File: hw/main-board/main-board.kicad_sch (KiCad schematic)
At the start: 66 parts, among them J1 USB_C_Receptacle_USB2.0_16P, J2 S4B-XH-A_LF__SN_, J3 S4B-XH-A_LF__SN_, J4 Conn_ARM_JTAG_SWD_10, Q1 AONR21307, U1 HUSB238_xxxDD, U2 AP63205WU, U3 AP2112K-3.3, U4 PTR54L, U5 TMC2226-SA, U6 TMC2226-SA, U7 KTD2026BEWE-TR

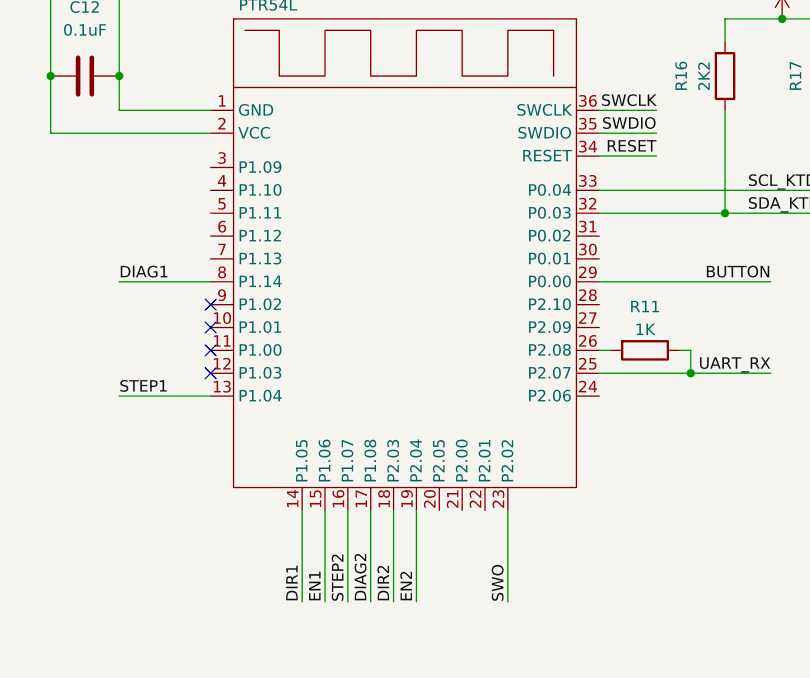
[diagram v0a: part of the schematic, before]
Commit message: Add not-connected labels
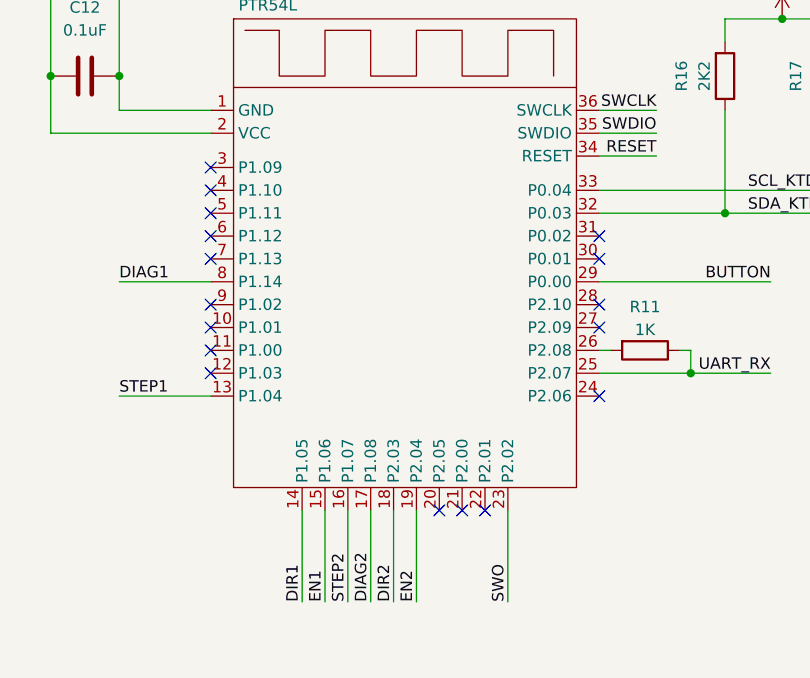
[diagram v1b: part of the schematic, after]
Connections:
- no-connect marks 16 -> 29
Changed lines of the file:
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@@
+	)
+	(no_connect
+		(at 243.84 63.5)
 	)
 	(no_connect
 		(at 92.71 109.22)
+	)
+	(no_connect
+		(at 287.02 88.9)
 	)
 	(no_connect
@@
 	)
 	(no_connect
+		(at 243.84 71.12)
+	)
+	(no_connect
+		(at 243.84 66.04)
+	)
+	(no_connect
+		(at 274.32 101.6)
+	)
+	(no_connect
+		(at 269.24 101.6)
+	)
+	(no_connect
+		(at 243.84 68.58)
+	)
+	(no_connect
 		(at 316.23 213.36)
 	)
@@
 	)
 	(no_connect
+		(at 271.78 101.6)
+	)
+	(no_connect
 		(at 243.84 83.82)
+	)
+	(no_connect
+		(at 287.02 73.66)
 	)
 	(no_connect
@@
 	)
 	(no_connect
+		(at 243.84 73.66)
+	)
+	(no_connect
+		(at 287.02 78.74)
+	)
+	(no_connect
 		(at 215.9 231.14)
 	)
@@
 	)
 	(no_connect
+		(at 287.02 81.28)
+	)
+	(no_connect
+		(at 287.02 71.12)
+	)
+	(no_connect

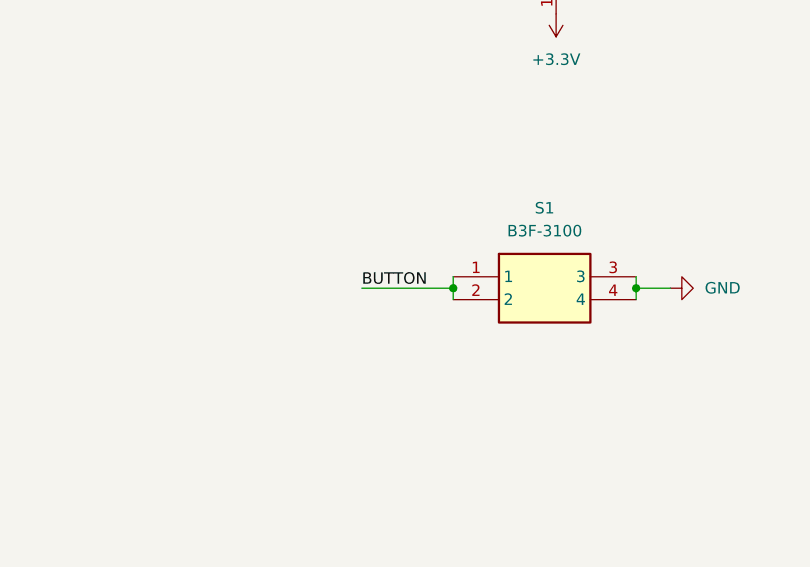
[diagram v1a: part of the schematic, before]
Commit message: Fix button pinout
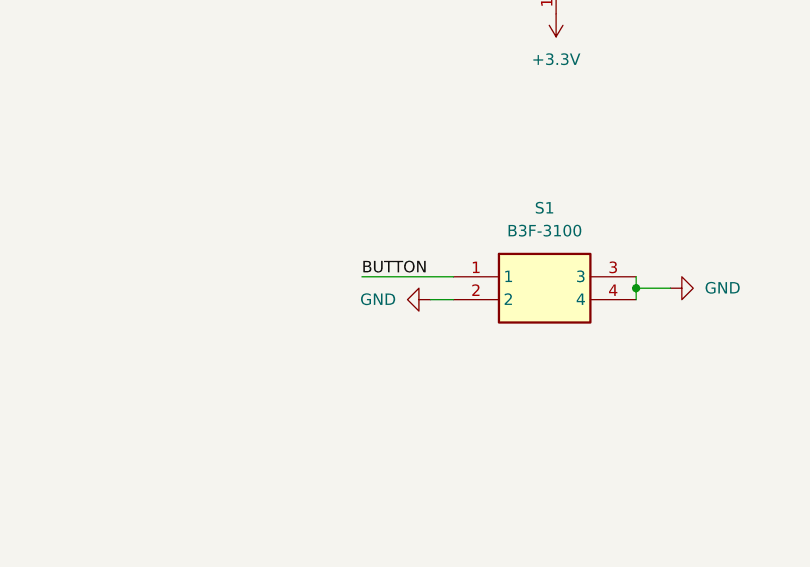
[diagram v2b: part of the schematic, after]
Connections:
- net BUTTON: no longer S1.2
- net GND: now also S1.2
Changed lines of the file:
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@@
 	)
 	(junction
-		(at 356.87 107.95)
-		(diameter 0)
-		(color 0 0 0 0)
-	)
-	(junction
 		(at 96.52 80.01)
 		(diameter 0)
@@
 	(wire
 		(pts
-			(xy 356.87 107.95) (xy 356.87 109.22)
-		)
-		(stroke
-			(width 0)
-			(type default)
-		)
-	)
-	(wire
-		(pts
 			(xy 215.9 160.02) (xy 218.44 160.02)
 		)
@@
 	(wire
 		(pts
-			(xy 346.71 107.95) (xy 356.87 107.95)
-		)
-		(stroke
-			(width 0)
-			(type default)
-		)
-	)
-	(wire
-		(pts
 			(xy 346.71 182.88) (xy 368.3 182.88)
 		)
@@
 	(wire
 		(pts
-			(xy 60.96 152.4) (xy 68.58 152.4)
+			(xy 354.33 109.22) (xy 356.87 109.22)
 		)
 		(stroke
@@
 	(wire
 		(pts
-			(xy 229.87 215.9) (xy 228.6 215.9)
+			(xy 60.96 152.4) (xy 68.58 152.4)
 		)
 		(stroke
@@
 	(wire
 		(pts
-			(xy 50.8 152.4) (xy 60.96 152.4)
+			(xy 229.87 215.9) (xy 228.6 215.9)
 		)
 		(stroke
@@
 	(wire
 		(pts
-			(xy 300.99 49.53) (xy 300.99 46.99)
+			(xy 50.8 152.4) (xy 60.96 152.4)
 		)
 		(stroke
@@
 	(wire
 		(pts
-			(xy 350.52 160.02) (xy 363.22 160.02)
+			(xy 300.99 49.53) (xy 300.99 46.99)
 		)
 		(stroke
@@
 	(wire
 		(pts
-			(xy 77.47 232.41) (xy 81.28 232.41)
+			(xy 350.52 160.02) (xy 363.22 160.02)
 		)
 		(stroke
@@
 	(wire
 		(pts
-			(xy 129.54 152.4) (xy 129.54 154.94)
+			(xy 77.47 232.41) (xy 81.28 232.41)
 		)
 		(stroke
@@
 	(wire
 		(pts
-			(xy 356.87 106.68) (xy 356.87 107.95)
+			(xy 129.54 152.4) (xy 129.54 154.94)
 		)
 		(stroke
@@
 	(wire
 		(pts
+			(xy 346.71 106.68) (xy 356.87 106.68)
+		)
+		(stroke
+			(width 0)
+			(type default)
+		)
+	)
+	(wire
+		(pts
 			(xy 250.19 187.96) (xy 250.19 189.23)
 		)
@@
 	)
 	(label "BUTTON"
-		(at 346.71 107.95 0)
+		(at 346.71 106.68 0)
 		(effects
 			(font
@@
 					(unit 1)
 				)
+			)
+		)
+	)
+	(symbol
+		(lib_id "power:GND")
+		(at 354.33 109.22 270)
+		(unit 1)
+		(body_style 1)
+		(exclude_from_sim no)
+		(in_bom yes)
+		(on_board yes)
+		(in_pos_files yes)
+		(dnp no)
+		(fields_autoplaced yes)
+		(property "Reference" "#PWR057"
+			(at 347.98 109.22 0)
+			(hide yes)
+			(show_name no)
+			(do_not_autoplace no)
+			(effects
+				(font
+					(size 1.27 1.27)
+				)
+			)
+		)
+		(property "Value" "GND"
+			(at 350.52 109.2199 90)
+			(show_name no)
+			(do_not_autoplace no)
+			(effects
+				(font
+					(size 1.27 1.27)
+				)
+				(justify right)
+			)
+		)
+		(property "Footprint" ""
+			(at 354.33 109.22 0)
+			(hide yes)
+			(show_name no)
+			(do_not_autoplace no)
+			(effects
+				(font
+					(size 1.27 1.27)
+				)
+			)
+		)
+		(property "Datasheet" ""
+			(at 354.33 109.22 0)
+			(hide yes)
+			(show_name no)
+			(do_not_autoplace no)
+			(effects
+				(font
+					(size 1.27 1.27)
+				)
+			)
+		)
+		(property "Description" "Power symbol creates a global label with name \"GND\" , ground"
+			(at 354.33 109.22 0)
+			(hide yes)
+			(show_name no)
+			(do_not_autoplace no)
+			(effects
+				(font
+					(size 1.27 1.27)
+				)
+			)
+		)
+		(pin "1"
+		)
+		(instances
+			(project "main-board"
+				(path "/fe215afa-a228-4dbb-8560-a0753323a3f2"
+					(reference "#PWR057")
+					(unit 1)
+				)

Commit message: Fix LED power source
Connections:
- net +3.3V: no longer C36.1, LED1.1, U7.5 (VIN)
- net +5V: now also C36.1, LED1.1, U7.5 (VIN)
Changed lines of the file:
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@@
 	)
 	(junction
-		(at 133.35 119.38)
-		(diameter 0)
-		(color 0 0 0 0)
-	)
-	(junction
 		(at 135.89 44.45)
 		(diameter 0)
@@
 	)
 	(junction
+		(at 133.35 119.38)
+		(diameter 0)
+		(color 0 0 0 0)
+	)
+	(junction
 		(at 50.8 160.02)
 		(diameter 0)
@@
 	)
 	(symbol
+		(lib_id "power:+5V")
+		(at 133.35 119.38 270)
+		(unit 1)
+		(body_style 1)
+		(exclude_from_sim no)
+		(in_bom yes)
+		(on_board yes)
+		(in_pos_files yes)
+		(dnp no)
+		(fields_autoplaced yes)
+		(property "Reference" "#PWR051"
+			(at 129.54 119.38 0)
+			(hide yes)
+			(show_name no)
+			(do_not_autoplace no)
+			(effects
+				(font
+					(size 1.27 1.27)
+				)
+			)
+		)
+		(property "Value" "+5V"
+			(at 137.16 119.3799 90)
+			(show_name no)
+			(do_not_autoplace no)
+			(effects
+				(font
+					(size 1.27 1.27)
+				)
+				(justify left)
+			)
+		)
+		(property "Footprint" ""
+			(at 133.35 119.38 0)
+			(hide yes)
+			(show_name no)
+			(do_not_autoplace no)
+			(effects
+				(font
+					(size 1.27 1.27)
+				)
+			)
+		)
+		(property "Datasheet" ""
+			(at 133.35 119.38 0)
+			(hide yes)
+			(show_name no)
+			(do_not_autoplace no)
+			(effects
+				(font
+					(size 1.27 1.27)
+				)
+			)
+		)
+		(property "Description" "Power symbol creates a global label with name \"+5V\""
+			(at 133.35 119.38 0)
+			(hide yes)
+			(show_name no)
+			(do_not_autoplace no)
+			(effects
+				(font
+					(size 1.27 1.27)
+				)
+			)
+		)
+		(pin "1"
+		)
+		(instances
+			(project "main-board"
+				(path "/fe215afa-a228-4dbb-8560-a0753323a3f2"
+					(reference "#PWR051")
+					(unit 1)
+				)
+			)
+		)
+	)
+	(symbol
 		(lib_id "power:GND")
 		(at 350.52 166.37 180)
@@
 	)
 	(symbol
+		(lib_id "power:+5V")
+		(at 186.69 124.46 270)
+		(unit 1)
+		(body_style 1)
+		(exclude_from_sim no)
+		(in_bom yes)
+		(on_board yes)
+		(in_pos_files yes)
+		(dnp no)
+		(fields_autoplaced yes)
+		(property "Reference" "#PWR052"
+			(at 182.88 124.46 0)
+			(hide yes)
+			(show_name no)
+			(do_not_autoplace no)
+			(effects
+				(font
+					(size 1.27 1.27)
+				)
+			)
+		)
+		(property "Value" "+5V"
+			(at 190.5 124.4599 90)
+			(show_name no)
+			(do_not_autoplace no)
+			(effects
+				(font
+					(size 1.27 1.27)
+				)
+				(justify left)
+			)
+		)
+		(property "Footprint" ""
+			(at 186.69 124.46 0)
+			(hide yes)
+			(show_name no)
+			(do_not_autoplace no)
+			(effects
+				(font
+					(size 1.27 1.27)
+				)
+			)
+		)
+		(property "Datasheet" ""
+			(at 186.69 124.46 0)
+			(hide yes)
+			(show_name no)
+			(do_not_autoplace no)
+			(effects
+				(font
+					(size 1.27 1.27)
+				)
+			)
+		)
+		(property "Description" "Power symbol creates a global label with name \"+5V\""
+			(at 186.69 124.46 0)
+			(hide yes)
+			(show_name no)
+			(do_not_autoplace no)
+			(effects
+				(font
+					(size 1.27 1.27)
+				)
+			)
+		)
+		(pin "1"
+		)
+		(instances
+			(project "main-board"
+				(path "/fe215afa-a228-4dbb-8560-a0753323a3f2"
+					(reference "#PWR052")
+					(unit 1)
+				)
+			)
+		)
+	)
+	(symbol
 		(lib_id "power:+3.3V")
 		(at 226.06 41.91 90)
@@
 	)
 	(symbol
-		(lib_id "power:+3.3V")
-		(at 133.35 119.38 270)
-		(unit 1)
-		(body_style 1)
-		(exclude_from_sim no)
-		(in_bom yes)
-		(on_board yes)
-		(in_pos_files yes)
-		(dnp no)
-		(fields_autoplaced yes)
-		(property "Reference" "#PWR052"
-			(at 129.54 119.38 0)
-			(hide yes)
-			(show_name no)
-			(do_not_autoplace no)
-			(effects
-				(font
-					(size 1.27 1.27)
-				)
-			)
-		)
-		(property "Value" "+3.3V"
-			(at 137.16 119.3799 90)
-			(show_name no)
-			(do_not_autoplace no)
-			(effects
-				(font
-					(size 1.27 1.27)
-				)
-				(justify left)
-			)
-		)
-		(property "Footprint" ""
-			(at 133.35 119.38 0)
-			(hide yes)
-			(show_name no)
-			(do_not_autoplace no)
-			(effects
-				(font
-					(size 1.27 1.27)
-				)
-			)
-		)
-		(property "Datasheet" ""
-			(at 133.35 119.38 0)
-			(hide yes)
-			(show_name no)
-			(do_not_autoplace no)
-			(effects
-				(font
-					(size 1.27 1.27)
-				)
-			)
-		)
-		(property "Description" "Power symbol creates a global label with name \"+3.3V\""
-			(at 133.35 119.38 0)
-			(hide yes)
-			(show_name no)
-			(do_not_autoplace no)
-			(effects
-				(font
-					(size 1.27 1.27)
-				)
-			)
-		)
-		(pin "1"
-		)
-		(instances
-			(project "main-board"
-				(path "/fe215afa-a228-4dbb-8560-a0753323a3f2"
-					(reference "#PWR052")
-					(unit 1)
-				)
-			)
-		)
-	)
-	(symbol
 		(lib_id "power:GND")
 		(at 172.72 198.12 270)
@@
 					(unit 1)
 				)
-			)
-		)
-	)
-	(symbol
-		(lib_id "power:+3.3V")
-		(at 186.69 124.46 270)
-		(unit 1)
-		(body_style 1)
-		(exclude_from_sim no)
-		(in_bom yes)
-		(on_board yes)
-		(in_pos_files yes)
-		(dnp no)
-		(fields_autoplaced yes)
-		(property "Reference" "#PWR051"
-			(at 182.88 124.46 0)
-			(hide yes)
-			(show_name no)
-			(do_not_autoplace no)
-			(effects
-				(font
-					(size 1.27 1.27)
-				)
-			)
-		)
-		(property "Value" "+3.3V"
-			(at 190.5 124.4599 90)
-			(show_name no)
-			(do_not_autoplace no)
-			(effects
-				(font
-					(size 1.27 1.27)
-				)
-				(justify left)
-			)
-		)
-		(property "Footprint" ""
-			(at 186.69 124.46 0)
-			(hide yes)
-			(show_name no)
-			(do_not_autoplace no)
-			(effects
-				(font
-					(size 1.27 1.27)
-				)
-			)
-		)
-		(property "Datasheet" ""
-			(at 186.69 124.46 0)
-			(hide yes)
-			(show_name no)
-			(do_not_autoplace no)
-			(effects
-				(font
-					(size 1.27 1.27)
-				)
-			)
-		)
-		(property "Description" "Power symbol creates a global label with name \"+3.3V\""
-			(at 186.69 124.46 0)
-			(hide yes)
-			(show_name no)
-			(do_not_autoplace no)
-			(effects
-				(font
-					(size 1.27 1.27)
-				)
-			)
-		)
-		(pin "1"
-		)
-		(instances
-			(project "main-board"
-				(path "/fe215afa-a228-4dbb-8560-a0753323a3f2"
-					(reference "#PWR051")
-					(unit 1)
-				)

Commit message: Add TVS and diodes for curcuit protection
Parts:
- added D1: SMBJ16A, DIOM5436X261N, symbol Samacsys:SMBJ16A
- added D2: SS34, Diode_SMD:D_SMA, symbol Diode:SS34
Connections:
- net GND: now also D1.2 (A)
- net VBUS: now also D1.1 (K), D2.1 (K); no longer Q1.5 (D_1), Q1.6 (D_2), Q1.7 (D_3), Q1.8 (D_4)
- new net: D2.2 (A), Q1.5 (D_1), Q1.6 (D_2), Q1.7 (D_3), Q1.8 (D_4)

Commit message: Add VSET resistor for HUSB238
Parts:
- R4: value 10R -> 14K; now fitted
- R5: value 10R -> 16K5
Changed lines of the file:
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@@
 			)
 		)
-		(property "Value" "10R"
+		(property "Value" "16K5"
 			(at 93.98 76.1999 0)
 			(show_name no)
@@
 		(in_bom yes)
 		(on_board yes)
-		(in_pos_files no)
-		(dnp yes)
+		(in_pos_files yes)
+		(dnp no)
 		(fields_autoplaced yes)
 		(property "Reference" "R4"
@@
 			)
 		)
-		(property "Value" "10R"
+		(property "Value" "14K"
 			(at 104.14 76.1999 0)
 			(show_name no)

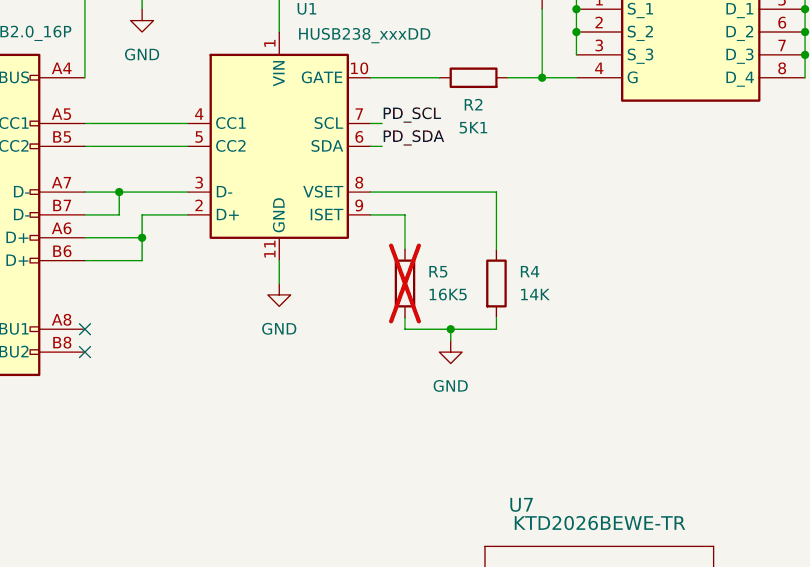
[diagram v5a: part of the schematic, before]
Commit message: Add ISET resistor for HUSB238
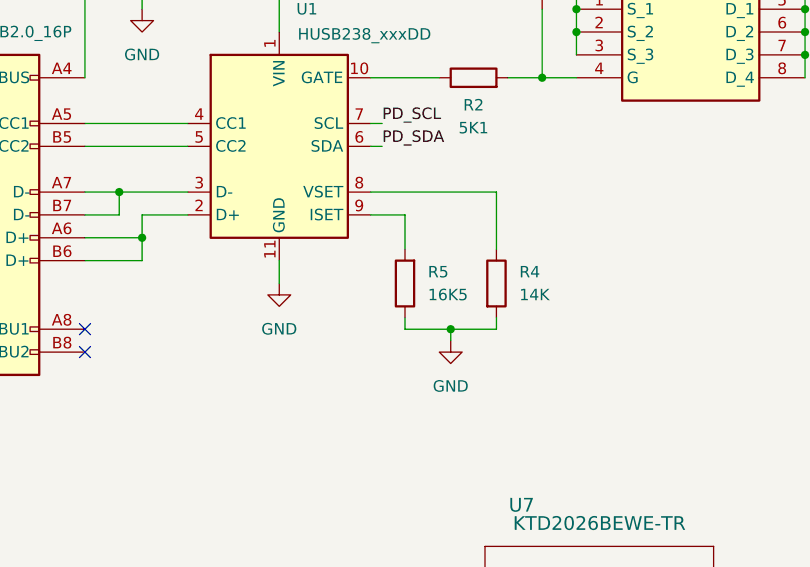
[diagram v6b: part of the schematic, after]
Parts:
- R5: now fitted
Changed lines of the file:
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@@
 		(in_bom yes)
 		(on_board yes)
-		(in_pos_files no)
-		(dnp yes)
+		(in_pos_files yes)
+		(dnp no)
 		(fields_autoplaced yes)
 		(property "Reference" "R5"
